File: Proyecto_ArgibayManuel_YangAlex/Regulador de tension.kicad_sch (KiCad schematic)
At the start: 0 parts

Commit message: arreglar errores con los esquematicos
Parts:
- added C10, C8: 1uF, symbol Device:C_Polarized_US
- added C11, C7, C9: 100nF, symbol Device:C
- added D3: 1N4002, Diode_THT:D_DO-41_SOD81_P10.16mm_Horizontal, symbol Diode:1N4002
- added D4: BZV55C6V2, Diode_SMD:D_MiniMELF, symbol Diode:BZV55C6V2
- added IC1: LM1117, symbol LM1117:LM1117
- added R11, R12: 1k, symbol Device:R
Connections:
- new net: C7.1, C8.1, D3.1 (K), D4.1 (K), IC1.3
- new net: C9.1, IC1.1, R11.1, R12.2
- new net GND: C10.2, C11.2, C9.2, R12.1
- new net GNDPWR: C7.2, C8.2, D4.2 (A)
- new net VBat: D3.2 (A)
- new net VCC: C10.1, C11.1, IC1.4, R11.2
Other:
- note added: "Regulador de Tensión LM1117"

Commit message: sensor
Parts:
- C10, C11, C7, C8, C9: footprint (none) -> Capacitor_SMD:C_0805_2012Metric
- IC1: footprint (none) -> LM1117:SOT223
- R11, R12: footprint (none) -> Resistor_THT:R_Axial_DIN0204_L3.6mm_D1.6mm_P1.90mm_Vertical
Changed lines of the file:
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@@
+	)
+	(symbol
+		(lib_id "LM1117:LM1117")
+		(at 80.01 39.37 0)
+		(unit 1)
+		(exclude_from_sim no)
+		(in_bom yes)
+		(on_board yes)
+		(dnp no)
+		(fields_autoplaced yes)
+		(property "Reference" "IC1"
+			(at 80.3354 31.75 0)
+			(effects
+				(font
+					(size 1.27 1.27)
+				)
+			)
+		)
+		(property "Value" "LM1117"
+			(at 80.3354 34.29 0)
+			(effects
+				(font
+					(size 1.27 1.27)
+				)
+			)
+		)
+		(property "Footprint" "LM1117:SOT223"
+			(at 80.01 39.37 0)
+			(effects
+				(font
+					(size 1.27 1.27)
+				)
+				(hide yes)
+			)
+		)
+		(property "Datasheet" ""
+			(at 80.01 39.37 0)
+			(effects
+				(font
+					(size 1.27 1.27)
+				)
+				(hide yes)
+			)
+		)
+		(property "Description" ""
+			(at 80.01 39.37 0)
+			(effects
+				(font
+					(size 1.27 1.27)
+				)
+				(hide yes)
+			)
+		)
+		(property "MF" "Texas Instruments"
+			(at 80.01 39.37 0)
+			(effects
+				(font
+					(size 1.27 1.27)
+				)
+				(justify bottom)
+				(hide yes)
+			)
+		)
+		(property "Description_1" "1A Low Dropout Positive Voltage Regulator"
+			(at 80.01 39.37 0)
+			(effects
+				(font
+					(size 1.27 1.27)
+				)
+				(justify bottom)
+				(hide yes)
+			)
+		)
+		(property "Package" "None"
+			(at 80.01 39.37 0)
+			(effects
+				(font
+					(size 1.27 1.27)
+				)
+				(justify bottom)
+				(hide yes)
+			)
+		)
+		(property "Price" "None"
+			(at 80.01 39.37 0)
+			(effects
+				(font
+					(size 1.27 1.27)
+				)
+				(justify bottom)
+				(hide yes)
+			)
+		)
+		(property "SnapEDA_Link" "https://www.snapeda.com/parts/LM1117/Texas+Instruments/view-part/?ref=snap"
+			(at 80.01 39.37 0)
+			(effects
+				(font
+					(size 1.27 1.27)
+				)
+				(justify bottom)
+				(hide yes)
+			)
+		)
+		(property "MP" "LM1117"
+			(at 80.01 39.37 0)
+			(effects
+				(font
+					(size 1.27 1.27)
+				)
+				(justify bottom)
+				(hide yes)
+			)
+		)
+		(property "Availability" "Not in stock"
+			(at 80.01 39.37 0)
+			(effects
+				(font
+					(size 1.27 1.27)
+				)
+				(justify bottom)
+				(hide yes)
+			)
+		)
+		(property "Check_prices" "https://www.snapeda.com/parts/LM1117/Texas+Instruments/view-part/?ref=eda"
+			(at 80.01 39.37 0)
+			(effects
+				(font
+					(size 1.27 1.27)
+				)
+				(justify bottom)
+				(hide yes)
+			)
+		)
+		(pin "1"
+		)
+		(pin "3"
+		)
+		(pin "4"
+		)
+		(instances
+			(project ""
+				(path "/b2dde924-33f5-41ab-a1bf-811873450a89/586cebd2-39d7-435a-989d-0b17f5522a13"
+					(reference "IC1")
+					(unit 1)
+				)
+			)
+		)
 	)
 	(symbol
@@
 			)
 		)
-		(property "Footprint" ""
+		(property "Footprint" "Capacitor_SMD:C_0805_2012Metric"
 			(at 55.5752 48.26 0)
 			(effects
@@
 	)
 	(symbol
-		(lib_id "LM1117:LM1117")
-		(at 80.01 39.37 0)
-		(unit 1)
-		(exclude_from_sim no)
-		(in_bom yes)
-		(on_board yes)
-		(dnp no)
-		(property "Reference" "IC1"
-			(at 80.01 31.496 0)
-			(effects
-				(font
-					(size 1.27 1.27)
-				)
-			)
-		)
-		(property "Value" "LM1117"
-			(at 80.3354 34.29 0)
-			(effects
-				(font
-					(size 1.27 1.27)
-				)
-			)
-		)
-		(property "Footprint" ""
-			(at 80.01 39.37 0)
-			(effects
-				(font
-					(size 1.27 1.27)
-				)
-				(hide yes)
-			)
-		)
-		(property "Datasheet" ""
-			(at 80.01 39.37 0)
-			(effects
-				(font
-					(size 1.27 1.27)
-				)
-				(hide yes)
-			)
-		)
-		(property "Description" ""
-			(at 80.01 39.37 0)
-			(effects
-				(font
-					(size 1.27 1.27)
-				)
-				(hide yes)
-			)
-		)
-		(property "MF" "Texas Instruments"
-			(at 80.01 39.37 0)
-			(effects
-				(font
-					(size 1.27 1.27)
-				)
-				(justify bottom)
-				(hide yes)
-			)
-		)
-		(property "Description_1" "1A Low Dropout Positive Voltage Regulator"
-			(at 80.01 39.37 0)
-			(effects
-				(font
-					(size 1.27 1.27)
-				)
-				(justify bottom)
-				(hide yes)
-			)
-		)
-		(property "Package" "None"
-			(at 80.01 39.37 0)
-			(effects
-				(font
-					(size 1.27 1.27)
-				)
-				(justify bottom)
-				(hide yes)
-			)
-		)
-		(property "Price" "None"
-			(at 80.01 39.37 0)
-			(effects
-				(font
-					(size 1.27 1.27)
-				)
-				(justify bottom)
-				(hide yes)
-			)
-		)
-		(property "SnapEDA_Link" "https://www.snapeda.com/parts/LM1117/Texas+Instruments/view-part/?ref=snap"
-			(at 80.01 39.37 0)
-			(effects
-				(font
-					(size 1.27 1.27)
-				)
-				(justify bottom)
-				(hide yes)
-			)
-		)
-		(property "MP" "LM1117"
-			(at 80.01 39.37 0)
-			(effects
-				(font
-					(size 1.27 1.27)
-				)
-				(justify bottom)
-				(hide yes)
-			)
-		)
-		(property "Availability" "Not in stock"
-			(at 80.01 39.37 0)
-			(effects
-				(font
-					(size 1.27 1.27)
-				)
-				(justify bottom)
-				(hide yes)
-			)
-		)
-		(property "Check_prices" "https://www.snapeda.com/parts/LM1117/Texas+Instruments/view-part/?ref=eda"
-			(at 80.01 39.37 0)
-			(effects
-				(font
-					(size 1.27 1.27)
-				)
-				(justify bottom)
-				(hide yes)
-			)
-		)
-		(pin "4"
-		)
-		(pin "3"
-		)
-		(pin "1"
-		)
-		(instances
-			(project "Proyecto_ArgibayManuel_YangAlex"
-				(path "/b2dde924-33f5-41ab-a1bf-811873450a89/586cebd2-39d7-435a-989d-0b17f5522a13"
-					(reference "IC1")
-					(unit 1)
-				)
-			)
-		)
-	)
-	(symbol
 		(lib_id "Device:C_Polarized_US")
 		(at 66.04 44.45 0)
@@
 			)
 		)
-		(property "Footprint" ""
+		(property "Footprint" "Capacitor_SMD:C_0805_2012Metric"
 			(at 66.04 44.45 0)
 			(effects
@@
 			)
 		)
-		(property "Footprint" ""
+		(property "Footprint" "Resistor_THT:R_Axial_DIN0204_L3.6mm_D1.6mm_P1.90mm_Vertical"
 			(at 93.218 44.45 90)
 			(effects
@@
 			)
 		)
-		(property "Footprint" ""
+		(property "Footprint" "Resistor_THT:R_Axial_DIN0204_L3.6mm_D1.6mm_P1.90mm_Vertical"
 			(at 93.218 55.88 90)
 			(effects
@@
 			)
 		)
-		(property "Footprint" ""
+		(property "Footprint" "Capacitor_SMD:C_0805_2012Metric"
 			(at 80.9752 59.69 0)
 			(effects
@@
 			)
 		)
-		(property "Footprint" ""
+		(property "Footprint" "Capacitor_SMD:C_0805_2012Metric"
 			(at 115.2652 48.26 0)
 			(effects
@@
 			)
 		)
-		(property "Footprint" ""
+		(property "Footprint" "Capacitor_SMD:C_0805_2012Metric"
 			(at 104.14 44.45 0)
 			(effects

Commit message: icsp
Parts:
- added R13: 0, Resistor_THT:R_Axial_DIN0204_L3.6mm_D1.6mm_P1.90mm_Vertical, symbol Device:R
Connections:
- net GND: now also R13.1
- net GNDPWR: now also R13.2
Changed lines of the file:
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@@
+	(wire
+		(pts
+			(xy 52.07 63.5) (xy 55.88 63.5)
+		)
+		(stroke
+			(width 0)
+			(type default)
+		)
+	)
 	(wire
 		(pts
@@
 	(wire
 		(pts
+			(xy 55.88 63.5) (xy 55.88 64.77)
+		)
+		(stroke
+			(width 0)
+			(type default)
+		)
+	)
+	(wire
+		(pts
 			(xy 91.44 39.37) (xy 91.44 40.64)
 		)
@@
 		(pts
 			(xy 66.04 39.37) (xy 66.04 40.64)
+		)
+		(stroke
+			(width 0)
+			(type default)
+		)
+	)
+	(wire
+		(pts
+			(xy 41.91 63.5) (xy 44.45 63.5)
 		)
 		(stroke
@@
 	)
 	(symbol
+		(lib_id "power:GND")
+		(at 55.88 64.77 0)
+		(unit 1)
+		(exclude_from_sim no)
+		(in_bom yes)
+		(on_board yes)
+		(dnp no)
+		(property "Reference" "#PWR039"
+			(at 55.88 71.12 0)
+			(effects
+				(font
+					(size 1.27 1.27)
+				)
+				(hide yes)
+			)
+		)
+		(property "Value" "GND"
+			(at 53.086 67.818 0)
+			(effects
+				(font
+					(size 1.27 1.27)
+				)
+			)
+		)
+		(property "Footprint" ""
+			(at 55.88 64.77 0)
+			(effects
+				(font
+					(size 1.27 1.27)
+				)
+				(hide yes)
+			)
+		)
+		(property "Datasheet" ""
+			(at 55.88 64.77 0)
+			(effects
+				(font
+					(size 1.27 1.27)
+				)
+				(hide yes)
+			)
+		)
+		(property "Description" "Power symbol creates a global label with name \"GND\" , ground"
+			(at 55.88 64.77 0)
+			(effects
+				(font
+					(size 1.27 1.27)
+				)
+				(hide yes)
+			)
+		)
+		(pin "1"
+		)
+		(instances
+			(project "Proyecto_ArgibayManuel_YangAlex"
+				(path "/b2dde924-33f5-41ab-a1bf-811873450a89/586cebd2-39d7-435a-989d-0b17f5522a13"
+					(reference "#PWR039")
+					(unit 1)
+				)
+			)
+		)
+	)
+	(symbol
 		(lib_id "power:GNDPWR")
 		(at 54.61 49.53 0)
@@
 	)
 	(symbol
+		(lib_id "Device:R")
+		(at 48.26 63.5 270)
+		(unit 1)
+		(exclude_from_sim no)
+		(in_bom yes)
+		(on_board yes)
+		(dnp no)
+		(fields_autoplaced yes)
+		(property "Reference" "R13"
+			(at 48.26 57.15 90)
+			(effects
+				(font
+					(size 1.27 1.27)
+				)
+			)
+		)
+		(property "Value" "0"
+			(at 48.26 59.69 90)
+			(effects
+				(font
+					(size 1.27 1.27)
+				)
+			)
+		)
+		(property "Footprint" "Resistor_THT:R_Axial_DIN0204_L3.6mm_D1.6mm_P1.90mm_Vertical"
+			(at 48.26 61.722 90)
+			(effects
+				(font
+					(size 1.27 1.27)
+				)
+				(hide yes)
+			)
+		)
+		(property "Datasheet" "~"
+			(at 48.26 63.5 0)
+			(effects
+				(font
+					(size 1.27 1.27)
+				)
+				(hide yes)
+			)
+		)
+		(property "Description" "Resistor"
+			(at 48.26 63.5 0)
+			(effects
+				(font
+					(size 1.27 1.27)
+				)
+				(hide yes)
+			)
+		)
+		(pin "1"
+		)
+		(pin "2"
+		)
+		(instances
+			(project "Proyecto_ArgibayManuel_YangAlex"
+				(path "/b2dde924-33f5-41ab-a1bf-811873450a89/586cebd2-39d7-435a-989d-0b17f5522a13"
+					(reference "R13")
+					(unit 1)
+				)
+			)
+		)
+	)
+	(symbol
 		(lib_id "Device:C_Polarized_US")
 		(at 66.04 44.45 0)
@@
 					(unit 1)
 				)
+			)
+		)
+	)
+	(symbol
+		(lib_id "power:GNDPWR")
+		(at 41.91 63.5 0)
+		(unit 1)
+		(exclude_from_sim no)
+		(in_bom yes)
+		(on_board yes)
+		(dnp no)
+		(fields_autoplaced yes)
+		(property "Reference" "#PWR038"
+			(at 41.91 68.58 0)
+			(effects
+				(font
+					(size 1.27 1.27)
+				)
+				(hide yes)
+			)
+		)
+		(property "Value" "GNDPWR"
+			(at 41.783 67.31 0)
+			(effects
+				(font
+					(size 1.27 1.27)
+				)
+			)
+		)
+		(property "Footprint" ""
+			(at 41.91 64.77 0)
+			(effects
+				(font
+					(size 1.27 1.27)
+				)
+				(hide yes)
+			)
+		)
+		(property "Datasheet" ""
+			(at 41.91 64.77 0)
+			(effects
+				(font
+					(size 1.27 1.27)
+				)
+				(hide yes)
+			)
+		)
+		(property "Description" "Power symbol creates a global label with name \"GNDPWR\" , global ground"
+			(at 41.91 63.5 0)
+			(effects
+				(font
+					(size 1.27 1.27)
+				)
+				(hide yes)
+			)
+		)
+		(pin "1"
+		)
+		(instances
+			(project "Proyecto_ArgibayManuel_YangAlex"
+				(path "/b2dde924-33f5-41ab-a1bf-811873450a89/586cebd2-39d7-435a-989d-0b17f5522a13"
+					(reference "#PWR038")
+					(unit 1)
+				)

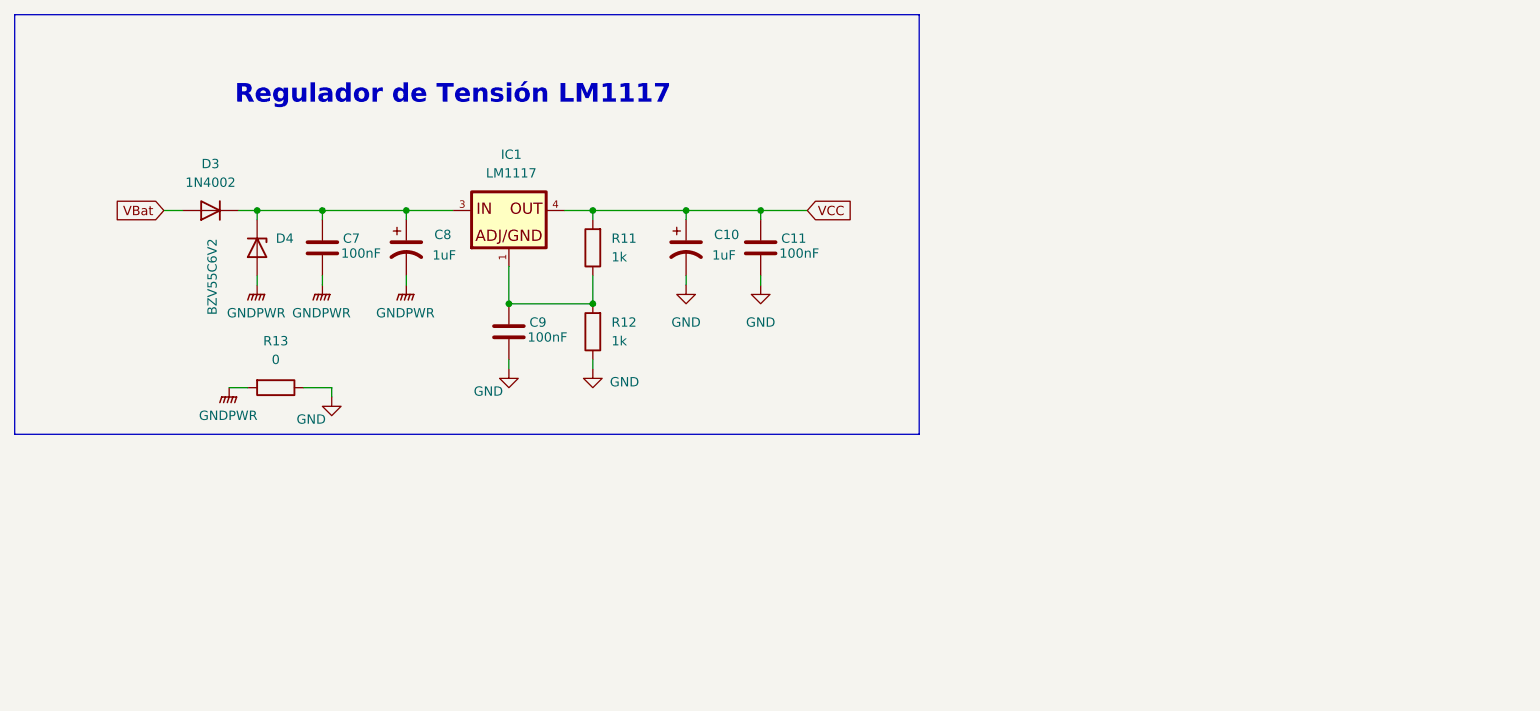
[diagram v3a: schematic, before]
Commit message: Arreglo net classes, agrego DB-9
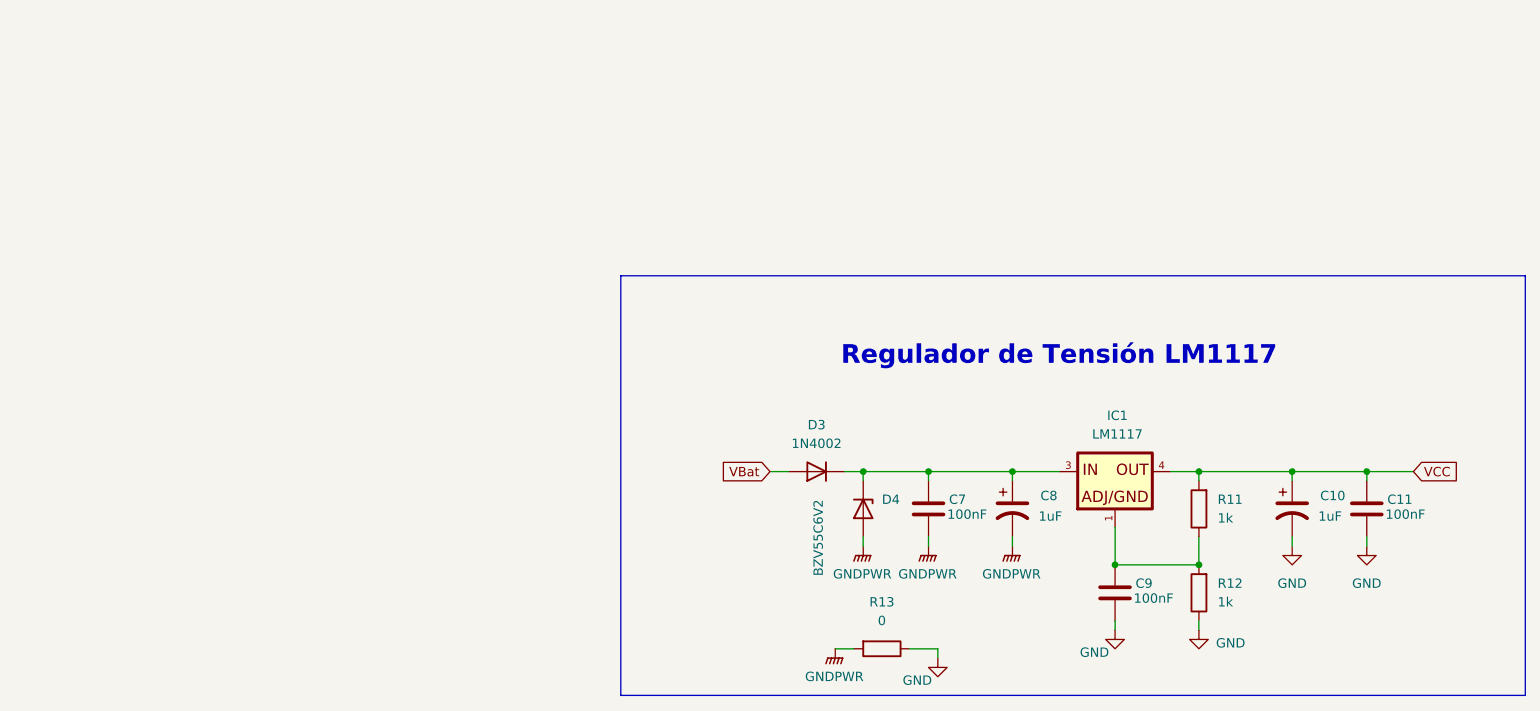
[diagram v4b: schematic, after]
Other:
- company: (none) -> Universidad de Barcelona
- title: (none) -> Regulador de tensión
- moved on the sheet: C10, C11, C7, C8, C9, D3, D4, IC1, R11, R12, R13
